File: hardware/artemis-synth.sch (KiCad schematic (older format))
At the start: 41 parts, among them J1 AVR-ISP-6, J2 CONN JACK STEREO R/A 3PIN 3.5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, SW1 SWITCH_PUSH_CW, SW10 SWITCH_PUSH_CW, SW2 SWITCH_PUSH_CW, SW3 SWITCH_PUSH_CW, SW4 SWITCH_PUSH_CW, SW5 SWITCH_PUSH_CW, SW6 SWITCH_PUSH_CW, SW7 SWITCH_PUSH_CW, SW8 SWITCH_PUSH_CW, SW9 SWITCH_PUSH_CW, U1 MCP4921, U2 ATMEGA328P

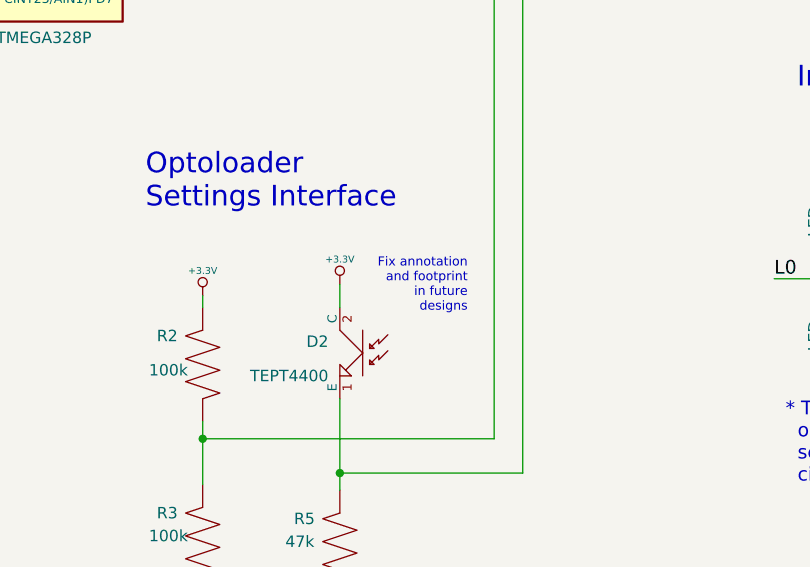
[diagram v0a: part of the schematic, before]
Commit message: reorganized firmware directory
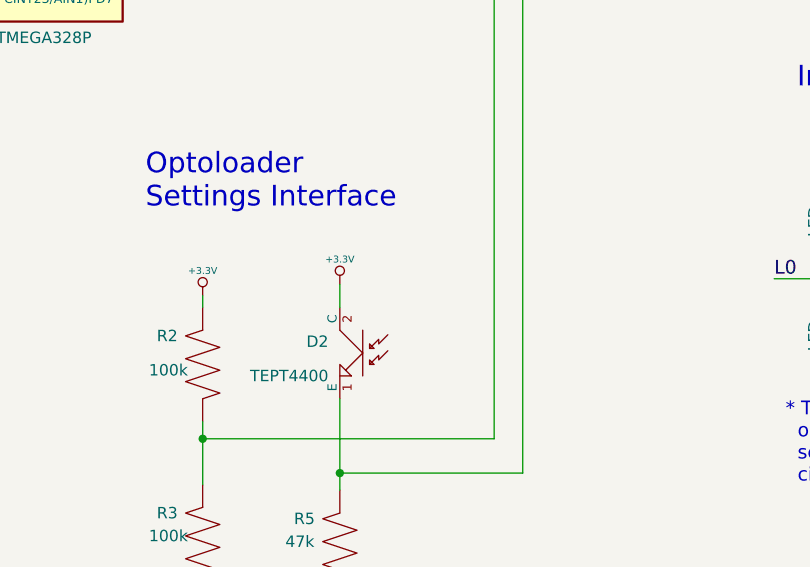
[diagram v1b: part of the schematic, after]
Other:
- note removed: "Fix annotation\nand footprint\nin future\ndesigns\n"
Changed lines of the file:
@@
-EESchema Schematic File Version 2  date Thu 11 Jul 2013 02:39:11 PM EDT
+EESchema Schematic File Version 2  date Thu 11 Jul 2013 03:24:18 PM EDT
 LIBS:power
 LIBS:device
@@
 	-1   0    0    -1
 $EndComp
-Text Notes 6409 5750 2    40   ~ 0
-Fix annotation\nand footprint\nin future\ndesigns\n
 $Comp
 L R_US R2
